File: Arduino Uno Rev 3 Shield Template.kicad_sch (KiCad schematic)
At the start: 4 parts, among them J1 Conn_01x08_Pin, J2 Conn_01x06_Pin, J3 Conn_01x08_Pin, J4 Conn_01x10_Pin

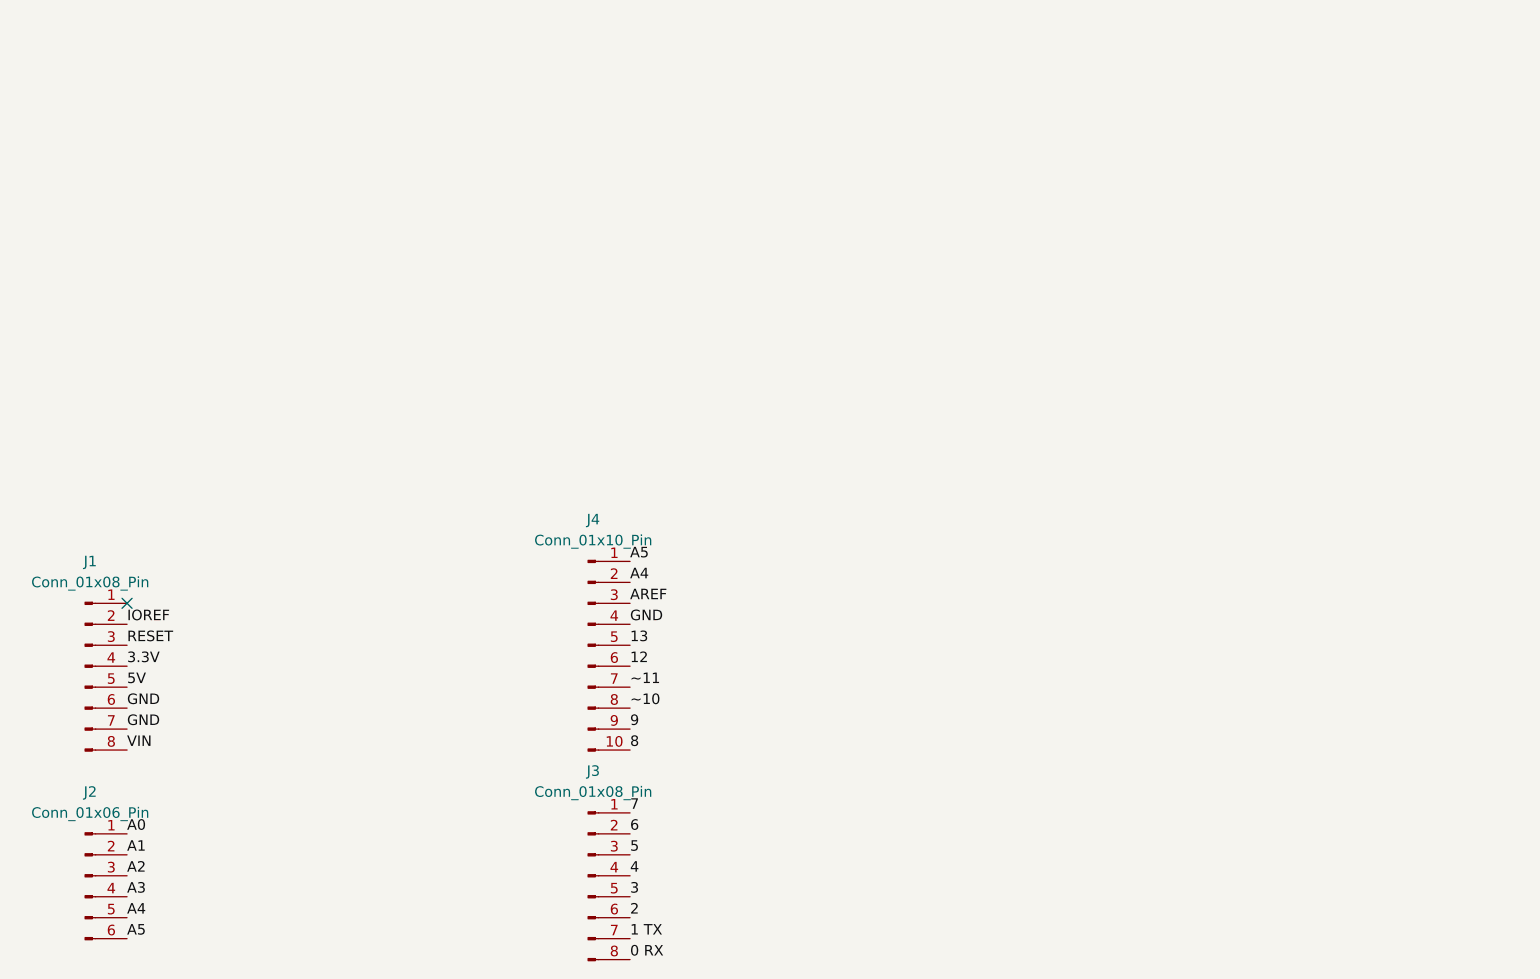
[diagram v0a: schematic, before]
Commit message: Added description and block to schematic
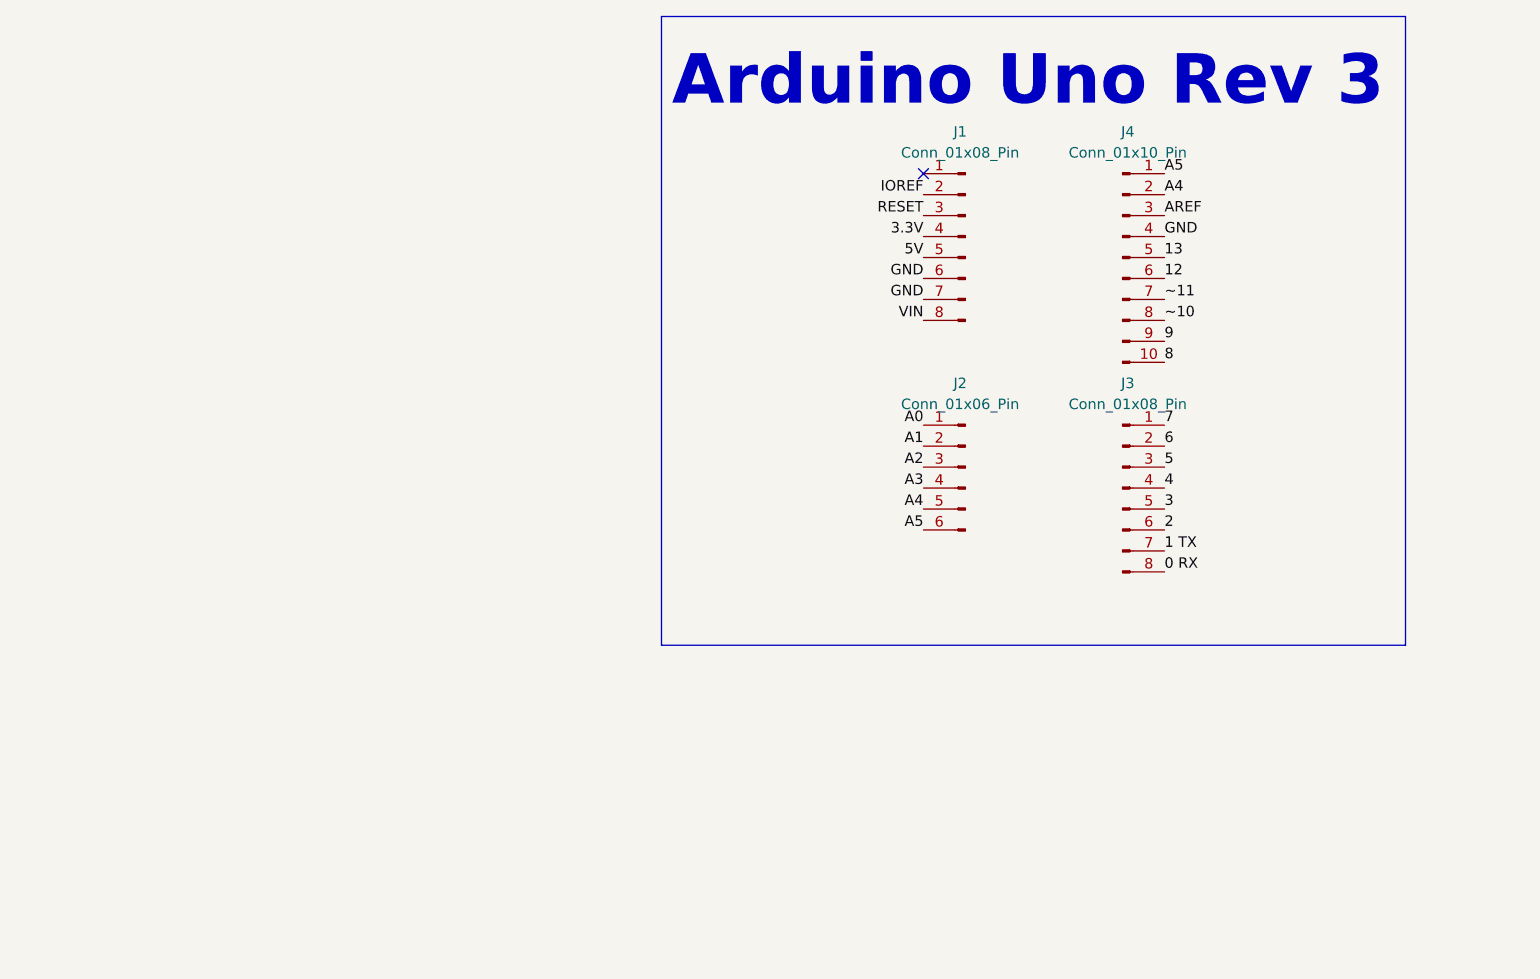
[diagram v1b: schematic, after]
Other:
- note added: "Arduino Uno Rev 3"
- moved on the sheet: J1, J2, J3, J4
